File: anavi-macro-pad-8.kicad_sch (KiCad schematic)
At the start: 45 parts, among them J1 USB_B_Micro, J2 Conn_01x04_Female, J3 Conn_01x03_Male, J4 Conn_01x03_Male, J5 AVR-ISP-6, Q1 Q_NPN_BEC, SW1 SW_DIP_x01, SW2 SW_DIP_x01, SW3 SW_DIP_x01, SW4 SW_DIP_x01, SW5 SW_DIP_x01, SW6 SW_DIP_x01, SW7 SW_DIP_x01, SW8 SW_DIP_x01, SW9 SW_DIP_x01, U1 ATmega32U4-AU, Y1 Crystal

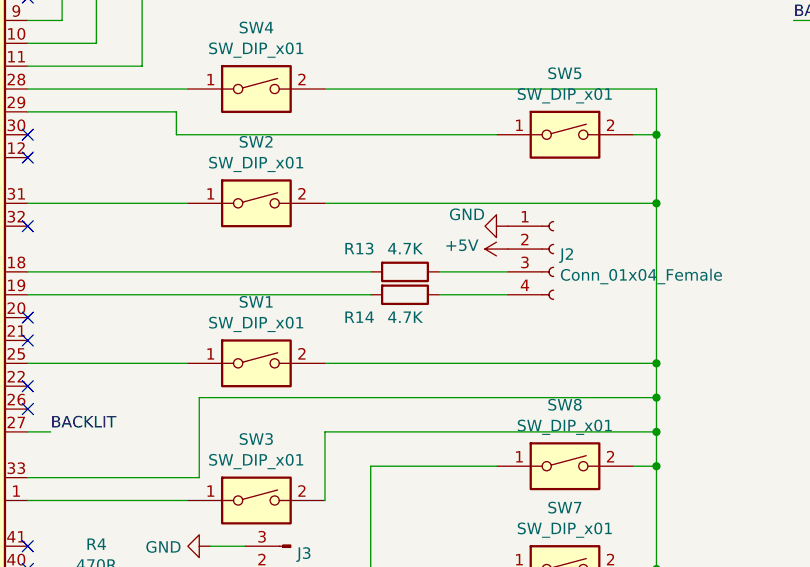
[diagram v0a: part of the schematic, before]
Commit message: anavi-macro-pad-8: Fix I2C protection resistors
Resistors R13 and R14 had too large values. These are protection
resistors used in series on the SDA and SCL lines of the I2C. To
fix this issue the values of both resistors were set to 24 Ohms.

fixes #4

Reported-by: Heiko Lau <h.lau@ifam-erfurt.de>
Signed-off-by: Leon Anavi <leon@anavi.org>
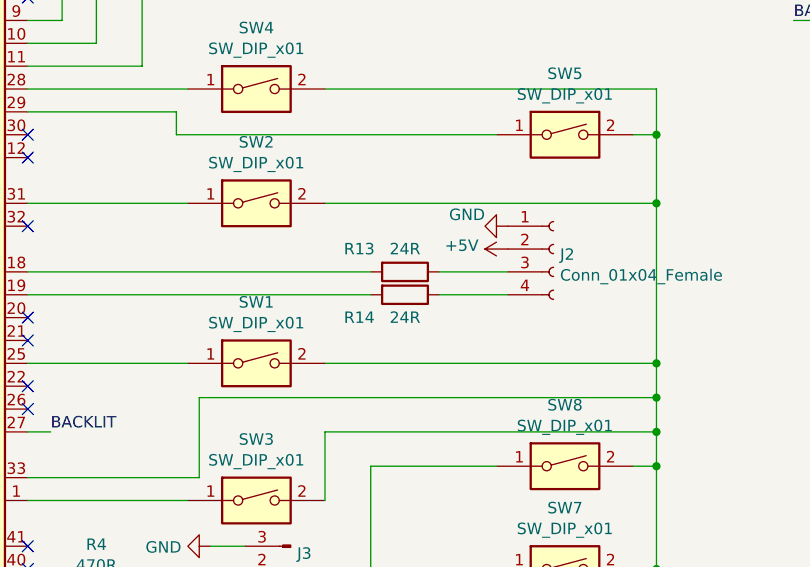
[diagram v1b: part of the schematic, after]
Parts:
- R13, R14: value 4.7K -> 24R
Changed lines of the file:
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@@
     (in_bom yes) (on_board yes)
     (property "Reference" "R13" (id 0) (at 162.56 86.36 90))
-    (property "Value" "4.7K" (id 1) (at 167.64 86.36 90))
+    (property "Value" "24R" (id 1) (at 167.64 86.36 90))
     (property "Footprint" "Resistors_SMD:R_0603" (id 2) (at 167.64 87.122 90)
       (effects (font (size 1.27 1.27)) hide)
@@
     (in_bom yes) (on_board yes)
     (property "Reference" "R14" (id 0) (at 162.56 93.98 90))
-    (property "Value" "4.7K" (id 1) (at 167.64 93.98 90))
+    (property "Value" "24R" (id 1) (at 167.64 93.98 90))
     (property "Footprint" "Resistors_SMD:R_0603" (id 2) (at 167.64 89.662 90)
       (effects (font (size 1.27 1.27)) hide)
@@
     )
     (path "/00000000-0000-0000-0000-00005eaf8e5f"
-      (reference "R13") (unit 1) (value "4.7K") (footprint "Resistors_SMD:R_0603")
+      (reference "R13") (unit 1) (value "24R") (footprint "Resistors_SMD:R_0603")
     )
     (path "/00000000-0000-0000-0000-00005eaf97ba"
-      (reference "R14") (unit 1) (value "4.7K") (footprint "Resistors_SMD:R_0603")
+      (reference "R14") (unit 1) (value "24R") (footprint "Resistors_SMD:R_0603")
     )
     (path "/00000000-0000-0000-0000-00005ead1f41"
